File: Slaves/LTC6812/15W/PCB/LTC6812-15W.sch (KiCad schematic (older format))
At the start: 55 parts, among them J1 Conn_01x01, J10 Slave, J11 Master, J2 Conn_01x01, J3 Conn_01x01, J4 Conn_01x01, J5 Cells, J6 Conn_01x10, Q1 DZTT5551, U1 LTC6812

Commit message: Readme changes
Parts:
- added C26, C27, C28, C29, C30, C31, C32, C33: 100n, Capacitors_SMD:C_0603_HandSoldering, symbol Device:C
- added R12, R16, R20, R24, R28, R32, R36, R40: 100k, Resistors_SMD:R_0603_HandSoldering, symbol Device:R
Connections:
- net GND: now also C26.2, C27.2, C28.2, C29.2, C30.2, C31.2, C32.2, C33.2
- net T2: now also C33.1, R40.2
- net T3: now also C32.1, R36.2
- net T4: now also C31.1, R32.2
- net T5: now also C30.1, R28.2
- net T6: now also C29.1, R24.2
- net T7: now also C28.1, R20.2
- net T8: now also C27.1, R16.2
- net T9: now also C26.1, R12.2
- net Vref2: now also R12.1, R16.1, R20.1, R24.1, R28.1, R32.1, R36.1, R40.1
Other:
- moved on the sheet: C8, C9, D4, J10, J11, J6, JP1, R10, R8, R9, TR1

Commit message: Datasheet update for V1.0
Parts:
- C1, C4: value 100nF -> 100n; MPN (none) -> GRM188R72A104KA35D
- C10, C26, C27, C28, C29, C30, C31, C32, C33: MPN (none) -> GRM188R72A104KA35D
- C2, C3, C5, C6, C7: MPN (none) -> CL10B105KP8NNNC
- C8, C9: MPN (none) -> GRM1885C1H101JA01D
- D1, D2: MPN (none) -> 1N4148W-7-F
- D3: MPN (none) -> BZT52H-C62
- FB1: MPN (none) -> BLM18PG330SN1D
- Q1: MPN (none) -> DZT5551-13
- R2: value 1k -> 806
- R5: value 1k -> 1.2
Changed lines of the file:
@@
 P 9650 2600
 F 0 "C4" H 9535 2554 50  0000 R CNN
-F 1 "100nF" H 9535 2645 50  0000 R CNN
+F 1 "100n" H 9535 2645 50  0000 R CNN
 F 2 "Capacitors_SMD:C_0603_HandSoldering" H 9688 2450 50  0001 C CNN
 F 3 "~" H 9650 2600 50  0001 C CNN
-F 4 "100V" H 9450 2750 50  0000 C CNN "Voltage"
+F 4 "GRM188R72A104KA35D" H 9650 2600 50  0001 C CNN "MPN"
+F 5 "100V" H 9450 2750 50  0000 C CNN "Voltage"
 	1    9650 2600
 	-1   0    0    1
@@
 F 2 "Capacitors_SMD:C_0603_HandSoldering" H 11138 3700 50  0001 C CNN
 F 3 "~" H 11100 3850 50  0001 C CNN
+F 4 "CL10B105KP8NNNC" H 11100 3850 50  0001 C CNN "MPN"
 	1    11100 3850
 	-1   0    0    1
@@
 P 9300 3000
 F 0 "R5" V 9093 3000 50  0000 C CNN
-F 1 "1k" V 9184 3000 50  0000 C CNN
+F 1 "1.2" V 9184 3000 50  0000 C CNN
 F 2 "Resistors_SMD:R_0603_HandSoldering" V 9230 3000 50  0001 C CNN
 F 3 "~" H 9300 3000 50  0001 C CNN
@@
 P 8750 3000
 F 0 "R2" V 8543 3000 50  0000 C CNN
-F 1 "1k" V 8634 3000 50  0000 C CNN
+F 1 "806" V 8634 3000 50  0000 C CNN
 F 2 "Resistors_SMD:R_0603_HandSoldering" V 8680 3000 50  0001 C CNN
 F 3 "~" H 8750 3000 50  0001 C CNN
@@
 F 2 "Capacitors_SMD:C_0603_HandSoldering" H 20038 3650 50  0001 C CNN
 F 3 "~" H 20000 3800 50  0001 C CNN
+F 4 "GRM1885C1H101JA01D" H 20000 3800 50  0001 C CNN "MPN"
 	1    20000 3800
 	0    -1   -1   0
@@
 F 2 "Capacitors_SMD:C_0603_HandSoldering" H 11538 3700 50  0001 C CNN
 F 3 "~" H 11500 3850 50  0001 C CNN
+F 4 "CL10B105KP8NNNC" H 11500 3850 50  0001 C CNN "MPN"
 	1    11500 3850
 	-1   0    0    1
@@
 F 2 "Capacitors_SMD:C_0603_HandSoldering" H 11938 3700 50  0001 C CNN
 F 3 "~" H 11900 3850 50  0001 C CNN
+F 4 "CL10B105KP8NNNC" H 11900 3850 50  0001 C CNN "MPN"
 	1    11900 3850
 	-1   0    0    1
@@
 F 2 "Capacitors_SMD:C_0603_HandSoldering" H 9088 1100 50  0001 C CNN
 F 3 "~" H 9050 1250 50  0001 C CNN
+F 4 "CL10B105KP8NNNC" H 9050 1250 50  0001 C CNN "MPN"
 	1    9050 1250
 	-1   0    0    1
@@
 F 2 "Capacitors_SMD:C_0603_HandSoldering" H 8538 1100 50  0001 C CNN
 F 3 "~" H 8500 1250 50  0001 C CNN
+F 4 "CL10B105KP8NNNC" H 8500 1250 50  0001 C CNN "MPN"
 	1    8500 1250
 	-1   0    0    1
@@
 F 2 "Capacitors_SMD:C_0603_HandSoldering" H 16038 12500 50  0001 C CNN
 F 3 "~" H 16000 12650 50  0001 C CNN
+F 4 "GRM188R72A104KA35D" H 16000 12650 50  0001 C CNN "MPN"
 	1    16000 12650
 	1    0    0    -1
@@
 P 5900 4900
 F 0 "C1" V 5648 4900 50  0000 C CNN
-F 1 "100nF" V 5739 4900 50  0000 C CNN
+F 1 "100n" V 5739 4900 50  0000 C CNN
 F 2 "Capacitors_SMD:C_0603_HandSoldering" H 5938 4750 50  0001 C CNN
 F 3 "~" H 5900 4900 50  0001 C CNN
-F 4 "100V" V 5550 4900 50  0000 C CNN "Voltage"
+F 4 "GRM188R72A104KA35D" V 5900 4900 50  0001 C CNN "MPN"
+F 5 "100V" V 5550 4900 50  0000 C CNN "Voltage"
 	1    5900 4900
 	-1   0    0    1
@@
 F 2 "Resistors_SMD:R_0603_HandSoldering" V 4730 4550 50  0001 C CNN
 F 3 "BLM18PG330SN1D" H 4800 4550 50  0001 C CNN
+F 4 "BLM18PG330SN1D" H 4800 4550 50  0001 C CNN "MPN"
 	1    4800 4550
 	0    1    1    0
@@
 F 2 "Diodes_SMD:D_SOD-123" H 3200 2675 50  0001 C CNN
 F 3 "https://www.vishay.com/docs/85748/1n4148w.pdf" H 3200 2850 50  0001 C CNN
+F 4 "1N4148W-7-F" H 3200 2850 50  0001 C CNN "MPN"
 	1    3200 2850
 	0    1    1    0
@@
 F 2 "Diodes_SMD:D_SOD-123" H 3700 2675 50  0001 C CNN
 F 3 "https://www.vishay.com/docs/85748/1n4148w.pdf" H 3700 2850 50  0001 C CNN
+F 4 "1N4148W-7-F" H 3700 2850 50  0001 C CNN "MPN"
 	1    3700 2850
 	0    1    1    0
@@
 F 2 "Diodes_SMD:D_SOD-123" H 4200 2675 50  0001 C CNN
 F 3 "https://diotec.com/tl_files/diotec/files/pdf/datasheets/bzt52b2v4.pdf" H 4200 2850 50  0001 C CNN
+F 4 "BZT52H-C62" H 4200 2850 50  0001 C CNN "MPN"
 	1    4200 2850
 	0    1    1    0
@@
 F 2 "TO_SOT_Packages_SMD:SOT-223" H 10800 3150 50  0001 C CNN
 F 3 "~" H 10600 3050 50  0001 C CNN
+F 4 "DZT5551-13 " H 10600 3050 50  0001 C CNN "MPN"
 	1    10600 3050
 	1    0    0    -1
@@
 F 2 "Capacitors_SMD:C_0603_HandSoldering" H 20038 3050 50  0001 C CNN
 F 3 "~" H 20000 3200 50  0001 C CNN
+F 4 "GRM1885C1H101JA01D" H 20000 3200 50  0001 C CNN "MPN"
 	1    20000 3200
 	0    -1   -1   0
@@
 F 2 "Capacitors_SMD:C_0603_HandSoldering" H 12588 5600 50  0001 C CNN
 F 3 "~" H 12550 5750 50  0001 C CNN
+F 4 "GRM188R72A104KA35D" H 12550 5750 50  0001 C CNN "MPN"
 	1    12550 5750
 	1    0    0    -1
@@
 F 2 "Capacitors_SMD:C_0603_HandSoldering" H 12938 5600 50  0001 C CNN
 F 3 "~" H 12900 5750 50  0001 C CNN
+F 4 "GRM188R72A104KA35D" H 12900 5750 50  0001 C CNN "MPN"
 	1    12900 5750
 	1    0    0    -1
@@
 F 2 "Capacitors_SMD:C_0603_HandSoldering" H 13288 5600 50  0001 C CNN
 F 3 "~" H 13250 5750 50  0001 C CNN
+F 4 "GRM188R72A104KA35D" H 13250 5750 50  0001 C CNN "MPN"
 	1    13250 5750
 	1    0    0    -1
@@
 F 2 "Capacitors_SMD:C_0603_HandSoldering" H 13638 5600 50  0001 C CNN
 F 3 "~" H 13600 5750 50  0001 C CNN
+F 4 "GRM188R72A104KA35D" H 13600 5750 50  0001 C CNN "MPN"
 	1    13600 5750
 	1    0    0    -1
@@
 F 2 "Capacitors_SMD:C_0603_HandSoldering" H 13988 5600 50  0001 C CNN
 F 3 "~" H 13950 5750 50  0001 C CNN
+F 4 "GRM188R72A104KA35D" H 13950 5750 50  0001 C CNN "MPN"
 	1    13950 5750
 	1    0    0    -1
@@
 F 2 "Capacitors_SMD:C_0603_HandSoldering" H 14338 5600 50  0001 C CNN
 F 3 "~" H 14300 5750 50  0001 C CNN
+F 4 "GRM188R72A104KA35D" H 14300 5750 50  0001 C CNN "MPN"
 	1    14300 5750
 	1    0    0    -1
@@
 F 2 "Capacitors_SMD:C_0603_HandSoldering" H 14688 5600 50  0001 C CNN
 F 3 "~" H 14650 5750 50  0001 C CNN
+F 4 "GRM188R72A104KA35D" H 14650 5750 50  0001 C CNN "MPN"
 	1    14650 5750
 	1    0    0    -1
@@
 F 2 "Capacitors_SMD:C_0603_HandSoldering" H 15038 5600 50  0001 C CNN
 F 3 "~" H 15000 5750 50  0001 C CNN
+F 4 "GRM188R72A104KA35D" H 15000 5750 50  0001 C CNN "MPN"
 	1    15000 5750
 	1    0    0    -1

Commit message: maintenance update
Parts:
- removed J6: Conn_01x10, Pin_Headers:Pin_Header_Angled_1x10_Pitch2.54mm, symbol Connector_Generic:Conn_01x10
- removed JP1: ~Last?, Pin_Headers:Pin_Header_Straight_1x02_Pitch2.54mm, symbol Device:Jumper
- added J6: Temp, Connector_PinHeader_2.54mm:PinHeader_1x09_P2.54mm_Horizontal, symbol Connector:Conn_01x09_Male
- C1, C10, C2, C26, C27, C28, C29, C3, C30, C31, C32, C33, C4, C5, C6, C7, C8, C9: footprint Capacitors_SMD:C_0603_HandSoldering -> Capacitor_SMD:C_0603_1608Metric
- D1, D2: footprint Diodes_SMD:D_SOD-123 -> Diode_SMD:D_SOD-123
- D3: value BZT52H-C62 -> MMSZ5268BT1G; footprint Diodes_SMD:D_SOD-123 -> Diode_SMD:D_SOD-123; MPN BZT52H-C62 -> MMSZ5268BT1G
- FB1, R1, R10, R11, R12, R16, R2, R20, R24, R28, R3, R32, R36, R4, R40, R5, R6, R7, R8, R9: footprint Resistors_SMD:R_0603_HandSoldering -> Resistor_SMD:R_0603_1608Metric
- J10, J11: footprint Connectors_Molex:Molex_KK-6410-02_02x2.54mm_Straight -> ENNOID:Pin_1x02-XL
- TH1: footprint Resistors_SMD:R_0805_HandSoldering -> Resistor_SMD:R_0805_2012Metric
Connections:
- net GND: now also J6.1 (Pin_1)
- net IPB: now also TR1.7
- net T2: now also J6.2 (Pin_2)
- net T3: now also J6.3 (Pin_3)
- net T4: now also J6.4 (Pin_4)
- net T5: now also J6.5 (Pin_5)
- net T6: now also J6.6 (Pin_6)
- net T7: now also J6.7 (Pin_7)
- net T8: now also J6.8 (Pin_8)
- net T9: now also J6.9 (Pin_9)
- net at TR1.1: now also J11.1 (Pin_1); no longer J11.2 (Pin_2)
- net at TR1.3: now also J11.2 (Pin_2); no longer J11.1 (Pin_1)
- net at TR1.4: now also J10.1 (Pin_1); no longer J10.2 (Pin_2)
- net at TR1.6: now also J10.2 (Pin_2); no longer J10.1 (Pin_1)

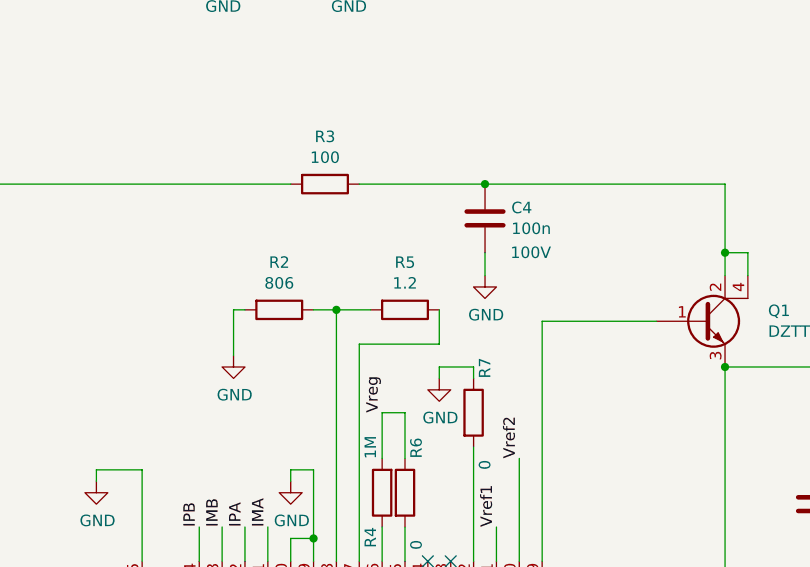
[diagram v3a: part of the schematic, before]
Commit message: Small changes to resistor & connectors
Now with vertical USB connectors & clip connectors
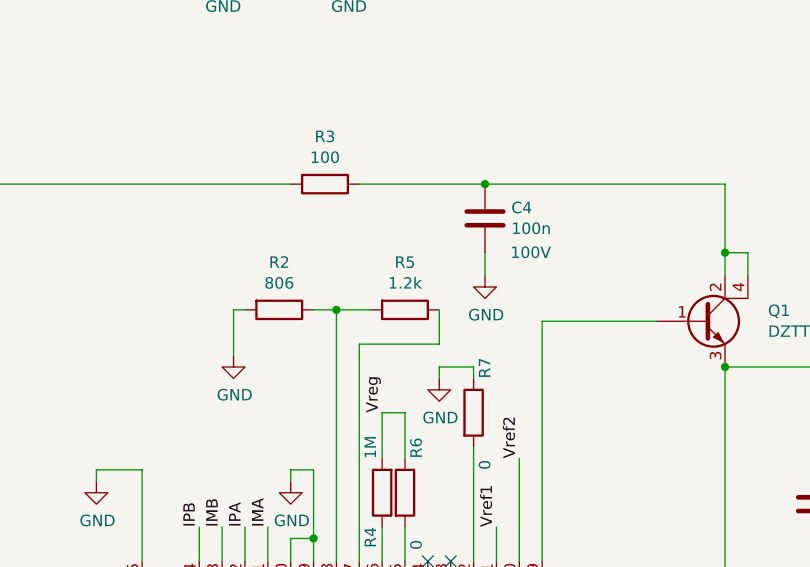
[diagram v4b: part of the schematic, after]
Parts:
- R5: value 1.2 -> 1.2k
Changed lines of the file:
@@
 P 9300 3000
 F 0 "R5" V 9093 3000 50  0000 C CNN
-F 1 "1.2" V 9184 3000 50  0000 C CNN
+F 1 "1.2k" V 9184 3000 50  0000 C CNN
 F 2 "Resistor_SMD:R_0603_1608Metric" V 9230 3000 50  0001 C CNN
 F 3 "~" H 9300 3000 50  0001 C CNN
@@
 F 1 "MMSZ5268BT1G " V 4245 2929 50  0000 L CNN
 F 2 "Diode_SMD:D_SOD-123" H 4200 2675 50  0001 C CNN
-F 3 "https://diotec.com/tl_files/diotec/files/pdf/datasheets/bzt52b2v4.pdf" H 4200 2850 50  0001 C CNN
+F 3 "" H 4200 2850 50  0001 C CNN
 F 4 "MMSZ5268BT1G" H 4200 2850 50  0001 C CNN "MPN"
 	1    4200 2850

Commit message: Schematics updates & improvements
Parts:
- J10: value Slave -> PB MB
- J11: value Master -> PA MA
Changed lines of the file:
@@
 P 21600 3850
 F 0 "J11" H 21680 3842 50  0000 L CNN
-F 1 "Master" H 21680 3751 50  0000 L CNN
+F 1 "PA MA" H 21680 3751 50  0000 L CNN
 F 2 "ENNOID:Pin_1x02-XL" H 21600 3850 50  0001 C CNN
 F 3 "~" H 21600 3850 50  0001 C CNN
@@
 P 21600 3250
 F 0 "J10" H 21680 3242 50  0000 L CNN
-F 1 "Slave" H 21680 3151 50  0000 L CNN
+F 1 "PB MB" H 21680 3151 50  0000 L CNN
 F 2 "ENNOID:Pin_1x02-XL" H 21600 3250 50  0001 C CNN
 F 3 "~" H 21600 3250 50  0001 C CNN
